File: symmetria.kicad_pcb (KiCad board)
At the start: 2 copper layers, 97 parts, among them J2 USB_C_Receptacle_USB2.0, SW1 SW_Push, U1 SRV05-4, U2 ATmega32U4-AU, Y1 16MHz

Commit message: PCB Laid out
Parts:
- added MX39: MX-NoLED, MX_Only:MXOnly-1.5U-NoLED, F.Cu at (774.7, 146.1)
- D1, D10, D11, D12, D13, D14, D15, D16, D17, D18, D19, D2, D20, D21, D22, D23, D24, D25, D26, D27, D28, D29, D3, D30, D31, D32, D33, D34, D35, D36, D37, D38, D39, D4, D5, D6, D7, D8, D9: moved to B.Cu
- moved D36 444.8 mm to (806.5, 127.0), turned to 90 degrees
- moved D24 439.4 mm to (806.5, 108.0), turned to 90 degrees
- moved D35 432.5 mm to (787.4, 127.0), turned to 90 degrees
- moved D12 431.7 mm to (806.5, 88.9), turned to 90 degrees
- moved D23 426.6 mm to (787.4, 108.0), turned to 90 degrees
- moved D39 424.8 mm to (782.6, 146.1), turned to 90 degrees
- moved D34 413.1 mm to (768.4, 127.0), turned to 90 degrees
- moved MX39 412.7 mm to (774.7, 146.1)
- moved MX36 411.8 mm to (798.5, 127.0)
- moved D11 408.1 mm to (787.4, 88.9), turned to 90 degrees
- moved D22 401.8 mm to (768.4, 108.0), turned to 90 degrees
- moved D10 396.5 mm to (768.4, 88.9), turned to 90 degrees
- moved MX24 392.2 mm to (798.5, 108.0)
- moved MX33 391.4 mm to (741.4, 127.0)
- moved MX34 386.9 mm to (760.4, 127.0)
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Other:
- board outline added: 254.4 x 90 mm

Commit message: PCB Laid out
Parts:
- moved R6 11.4 mm to (575.3, 84.5), turned to 180 degrees
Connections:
- net Net-(U2-Pad19) renamed ROW3
- U2 pad 20: Net-(U2-Pad20) -> ROW2
- U2 pad 21: Net-(U2-Pad21) -> ROW1
- U2 pad 22: Net-(U2-Pad22) -> ROW0
- U2 pad 25: Net-(U2-Pad25) -> COL0
- U2 pad 26: Net-(U2-Pad26) -> COL1
- U2 pad 27: Net-(U2-Pad27) -> COL2
- U2 pad 28: Net-(U2-Pad28) -> COL3
- U2 pad 29: Net-(U2-Pad29) -> COL4
- U2 pad 30: Net-(U2-Pad30) -> COL5
- U2 pad 31: Net-(U2-Pad31) -> COL6
- U2 pad 32: Net-(U2-Pad32) -> COL7
- U2 pad 36: Net-(U2-Pad36) -> COL8
- U2 pad 37: Net-(U2-Pad37) -> COL9
- U2 pad 38: Net-(U2-Pad38) -> COL10
- U2 pad 39: Net-(U2-Pad39) -> COL11
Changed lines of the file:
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@@
     (zones 0)
     (modules 98)
-    (nets 100)
+    (nets 85)
   )
   (page A4)
@@
   (net 75 "Net-(U2-Pad41)")
   (net 76 "Net-(U2-Pad40)")
-  (net 77 "Net-(U2-Pad39)")
-  (net 78 "Net-(U2-Pad38)")
-  (net 79 "Net-(U2-Pad37)")
-  (net 80 "Net-(U2-Pad36)")
-  (net 81 "Net-(U2-Pad32)")
-  (net 82 "Net-(U2-Pad31)")
-  (net 83 "Net-(U2-Pad30)")
-  (net 84 "Net-(U2-Pad29)")
-  (net 85 "Net-(U2-Pad28)")
-  (net 86 "Net-(U2-Pad27)")
-  (net 87 "Net-(U2-Pad26)")
-  (net 88 "Net-(U2-Pad25)")
-  (net 89 "Net-(U2-Pad22)")
-  (net 90 "Net-(U2-Pad21)")
-  (net 91 "Net-(U2-Pad20)")
-  (net 92 "Net-(U2-Pad19)")
-  (net 93 "Net-(U2-Pad18)")
-  (net 94 "Net-(U2-Pad12)")
-  (net 95 "Net-(U2-Pad11)")
-  (net 96 "Net-(U2-Pad10)")
-  (net 97 "Net-(U2-Pad9)")
-  (net 98 "Net-(U2-Pad8)")
-  (net 99 "Net-(U2-Pad1)")
+  (net 77 "Net-(U2-Pad18)")
+  (net 78 "Net-(U2-Pad12)")
+  (net 79 "Net-(U2-Pad11)")
+  (net 80 "Net-(U2-Pad10)")
+  (net 81 "Net-(U2-Pad9)")
+  (net 82 "Net-(U2-Pad8)")
+  (net 83 "Net-(U2-Pad1)")
+  (net 84 ROW3)
   (net_class Default "This is the default net class."
     (clearance 0.2)
@@
     (add_net "Net-(U2-Pad12)")
     (add_net "Net-(U2-Pad18)")
-    (add_net "Net-(U2-Pad19)")
-    (add_net "Net-(U2-Pad20)")
-    (add_net "Net-(U2-Pad21)")
-    (add_net "Net-(U2-Pad22)")
-    (add_net "Net-(U2-Pad25)")
-    (add_net "Net-(U2-Pad26)")
-    (add_net "Net-(U2-Pad27)")
-    (add_net "Net-(U2-Pad28)")
-    (add_net "Net-(U2-Pad29)")
-    (add_net "Net-(U2-Pad30)")
-    (add_net "Net-(U2-Pad31)")
-    (add_net "Net-(U2-Pad32)")
-    (add_net "Net-(U2-Pad36)")
-    (add_net "Net-(U2-Pad37)")
-    (add_net "Net-(U2-Pad38)")
-    (add_net "Net-(U2-Pad39)")
     (add_net "Net-(U2-Pad40)")
     (add_net "Net-(U2-Pad41)")
@@
     (add_net ROW1)
     (add_net ROW2)
+    (add_net ROW3)
     (add_net ROW4)
     (add_net VBUS)
@@
       (net 76 "Net-(U2-Pad40)"))
     (pad 39 smd rect (at 0 -5.7 90) (size 1.5 0.55) (layers F.Cu F.Paste F.Mask)
-      (net 77 "Net-(U2-Pad39)"))
+      (net 67 COL11))
     (pad 38 smd rect (at 0.8 -5.7 90) (size 1.5 0.55) (layers F.Cu F.Paste F.Mask)
-      (net 78 "Net-(U2-Pad38)"))
+      (net 66 COL10))
     (pad 37 smd rect (at 1.6 -5.7 90) (size 1.5 0.55) (layers F.Cu F.Paste F.Mask)
-      (net 79 "Net-(U2-Pad37)"))
+      (net 65 COL9))
     (pad 36 smd rect (at 2.4 -5.7 90) (size 1.5 0.55) (layers F.Cu F.Paste F.Mask)
-      (net 80 "Net-(U2-Pad36)"))
+      (net 64 COL8))
     (pad 35 smd rect (at 3.2 -5.7 90) (size 1.5 0.55) (layers F.Cu F.Paste F.Mask)
       (net 1 GND))
@@
       (net 73 "Net-(R6-Pad2)"))
     (pad 32 smd rect (at 5.7 -3.2) (size 1.5 0.55) (layers F.Cu F.Paste F.Mask)
-      (net 81 "Net-(U2-Pad32)"))
+      (net 63 COL7))
     (pad 31 smd rect (at 5.7 -2.4) (size 1.5 0.55) (layers F.Cu F.Paste F.Mask)
-      (net 82 "Net-(U2-Pad31)"))
+      (net 62 COL6))
     (pad 30 smd rect (at 5.7 -1.6) (size 1.5 0.55) (layers F.Cu F.Paste F.Mask)
-      (net 83 "Net-(U2-Pad30)"))
+      (net 61 COL5))
     (pad 29 smd rect (at 5.7 -0.8) (size 1.5 0.55) (layers F.Cu F.Paste F.Mask)
-      (net 84 "Net-(U2-Pad29)"))
+      (net 60 COL4))
     (pad 28 smd rect (at 5.7 0) (size 1.5 0.55) (layers F.Cu F.Paste F.Mask)
-      (net 85 "Net-(U2-Pad28)"))
+      (net 59 COL3))
     (pad 27 smd rect (at 5.7 0.8) (size 1.5 0.55) (layers F.Cu F.Paste F.Mask)
-      (net 86 "Net-(U2-Pad27)"))
+      (net 58 COL2))
     (pad 26 smd rect (at 5.7 1.6) (size 1.5 0.55) (layers F.Cu F.Paste F.Mask)
-      (net 87 "Net-(U2-Pad26)"))
+      (net 57 COL1))
     (pad 25 smd rect (at 5.7 2.4) (size 1.5 0.55) (layers F.Cu F.Paste F.Mask)
-      (net 88 "Net-(U2-Pad25)"))
+      (net 56 COL0))
     (pad 24 smd rect (at 5.7 3.2) (size 1.5 0.55) (layers F.Cu F.Paste F.Mask)
       (net 5 +5V))
@@
       (net 1 GND))
     (pad 22 smd rect (at 4 5.7 90) (size 1.5 0.55) (layers F.Cu F.Paste F.Mask)
-      (net 89 "Net-(U2-Pad22)"))
+      (net 7 ROW0))
     (pad 21 smd rect (at 3.2 5.7 90) (size 1.5 0.55) (layers F.Cu F.Paste F.Mask)
-      (net 90 "Net-(U2-Pad21)"))
+      (net 20 ROW1))
     (pad 20 smd rect (at 2.4 5.7 90) (size 1.5 0.55) (layers F.Cu F.Paste F.Mask)
-      (net 91 "Net-(U2-Pad20)"))
+      (net 33 ROW2))
     (pad 19 smd rect (at 1.6 5.7 90) (size 1.5 0.55) (layers F.Cu F.Paste F.Mask)
-      (net 92 "Net-(U2-Pad19)"))
+      (net 84 ROW3))
     (pad 18 smd rect (at 0.8 5.7 90) (size 1.5 0.55) (layers F.Cu F.Paste F.Mask)
-      (net 93 "Net-(U2-Pad18)"))
+      (net 77 "Net-(U2-Pad18)"))
     (pad 17 smd rect (at 0 5.7 90) (size 1.5 0.55) (layers F.Cu F.Paste F.Mask)
       (net 2 "Net-(C1-Pad1)"))
@@
       (net 68 "Net-(R3-Pad2)"))
     (pad 12 smd rect (at -4 5.7 90) (size 1.5 0.55) (layers F.Cu F.Paste F.Mask)
-      (net 94 "Net-(U2-Pad12)"))
+      (net 78 "Net-(U2-Pad12)"))
     (pad 11 smd rect (at -5.7 4) (size 1.5 0.55) (layers F.Cu F.Paste F.Mask)
-      (net 95 "Net-(U2-Pad11)"))
+      (net 79 "Net-(U2-Pad11)"))
     (pad 10 smd rect (at -5.7 3.2) (size 1.5 0.55) (layers F.Cu F.Paste F.Mask)
-      (net 96 "Net-(U2-Pad10)"))
+      (net 80 "Net-(U2-Pad10)"))
     (pad 9 smd rect (at -5.7 2.4) (size 1.5 0.55) (layers F.Cu F.Paste F.Mask)
-      (net 97 "Net-(U2-Pad9)"))
+      (net 81 "Net-(U2-Pad9)"))
     (pad 8 smd rect (at -5.7 1.6) (size 1.5 0.55) (layers F.Cu F.Paste F.Mask)
-      (net 98 "Net-(U2-Pad8)"))
+      (net 82 "Net-(U2-Pad8)"))
     (pad 7 smd rect (at -5.7 0.8) (size 1.5 0.55) (layers F.Cu F.Paste F.Mask)
       (net 5 +5V))
@@
       (net 5 +5V))
     (pad 1 smd rect (at -5.7 -4) (size 1.5 0.55) (layers F.Cu F.Paste F.Mask)
-      (net 99 "Net-(U2-Pad1)"))
+      (net 83 "Net-(U2-Pad1)"))
     (model ${KISYS3DMOD}/Package_QFP.3dshapes/TQFP-44_10x10mm_P0.8mm.wrl
       (at (xyz 0 0 0))
@@
   )
   (module Resistor_SMD:R_0805_2012Metric (layer F.Cu)
-    (at 575.183 95.8365 90)
+    (at 575.31 84.455 180)
     (descr "Resistor SMD 0805 (2012 Metric), square (rectangular) end terminal, IPC_7351 nominal, (Body size source: https://docs.google.com/spreadsheets/d/1BsfQQcO9C6DZCsRaXUlFlo91Tg2WpOkGARC1WS5S8t0/edit?usp=sharing), generated with kicad-footprint-generator")
     (tags resistor)
     (attr smd)
-    (fp_text reference R6 (at 0 -1.65 270) (layer F.SilkS)
-      (effects (font (size 1 1) (thickness 0.15)))
-    )
-    (fp_text value 10K (at 0 1.65 270) (layer F.Fab)
+    (fp_text reference R6 (at 0 -1.65 180) (layer F.SilkS)
+      (effects (font (size 1 1) (thickness 0.15)))
+    )
+    (fp_text value 10K (at 0 1.65 180) (layer F.Fab)
       (effects (font (size 1 1) (thickness 0.15)))
     )
@@
     (fp_line (start -1 -0.6) (end 1 -0.6) (layer F.Fab) (width 0.1))
     (fp_line (start -1 0.6) (end -1 -0.6) (layer F.Fab) (width 0.1))
-    (fp_text user %R (at 0 0 270) (layer F.Fab)
+    (fp_text user %R (at 0 0 180) (layer F.Fab)
       (effects (font (size 0.5 0.5) (thickness 0.08)))
     )
-    (pad 2 smd roundrect (at 0.9375 0 90) (size 0.975 1.4) (layers F.Cu F.Paste F.Mask) (roundrect_rratio 0.25)
+    (pad 2 smd roundrect (at 0.9375 0 180) (size 0.975 1.4) (layers F.Cu F.Paste F.Mask) (roundrect_rratio 0.25)
       (net 73 "Net-(R6-Pad2)"))
-    (pad 1 smd roundrect (at -0.9375 0 90) (size 0.975 1.4) (layers F.Cu F.Paste F.Mask) (roundrect_rratio 0.25)
+    (pad 1 smd roundrect (at -0.9375 0 180) (size 0.975 1.4) (layers F.Cu F.Paste F.Mask) (roundrect_rratio 0.25)
       (net 1 GND))
     (model ${KISYS3DMOD}/Resistor_SMD.3dshapes/R_0805_2012Metric.wrl

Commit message: Switch Tracing Complete
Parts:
- J2: moved to B.Cu
- moved C4 4.45 mm to (565.0, 112.3)
- turned J2 to 0 degrees
- turned U1 to 270 degrees
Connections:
- D37 pad 1: ROW4 -> ROW3
- D38 pad 1: ROW4 -> ROW3
- D39 pad 1: ROW4 -> ROW3
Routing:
- net COL10: track 0.00 -> 291.3 mm
- net COL11: track 0.00 -> 288.1 mm
- net ROW2: track 0.00 -> 283.2 mm, vias 0 -> 1
- net ROW1: track 0.00 -> 268.7 mm, vias 0 -> 1
- net ROW0: track 0.00 -> 266.7 mm, vias 0 -> 1
- net ROW3: track 0.00 -> 264.2 mm, vias 0 -> 1
- net COL9: track 0.00 -> 247.4 mm
- net COL8: track 0.00 -> 225.6 mm
- net COL6: track 0.00 -> 212.5 mm
- net COL7: track 0.00 -> 202.9 mm
- net COL5: track 0.00 -> 164.9 mm
- net COL4: track 0.00 -> 145.9 mm
- net COL3: track 0.00 -> 127.0 mm
- net COL1: track 0.00 -> 112.7 mm
- net COL2: track 0.00 -> 107.9 mm
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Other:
- outline, holes or cut-outs redrawn
- net class Default: trace_width 0.25 -> 0.254
- net class Power added: clearance 0.2, trace_width 0.381, via_dia 0.8, via_drill 0.4

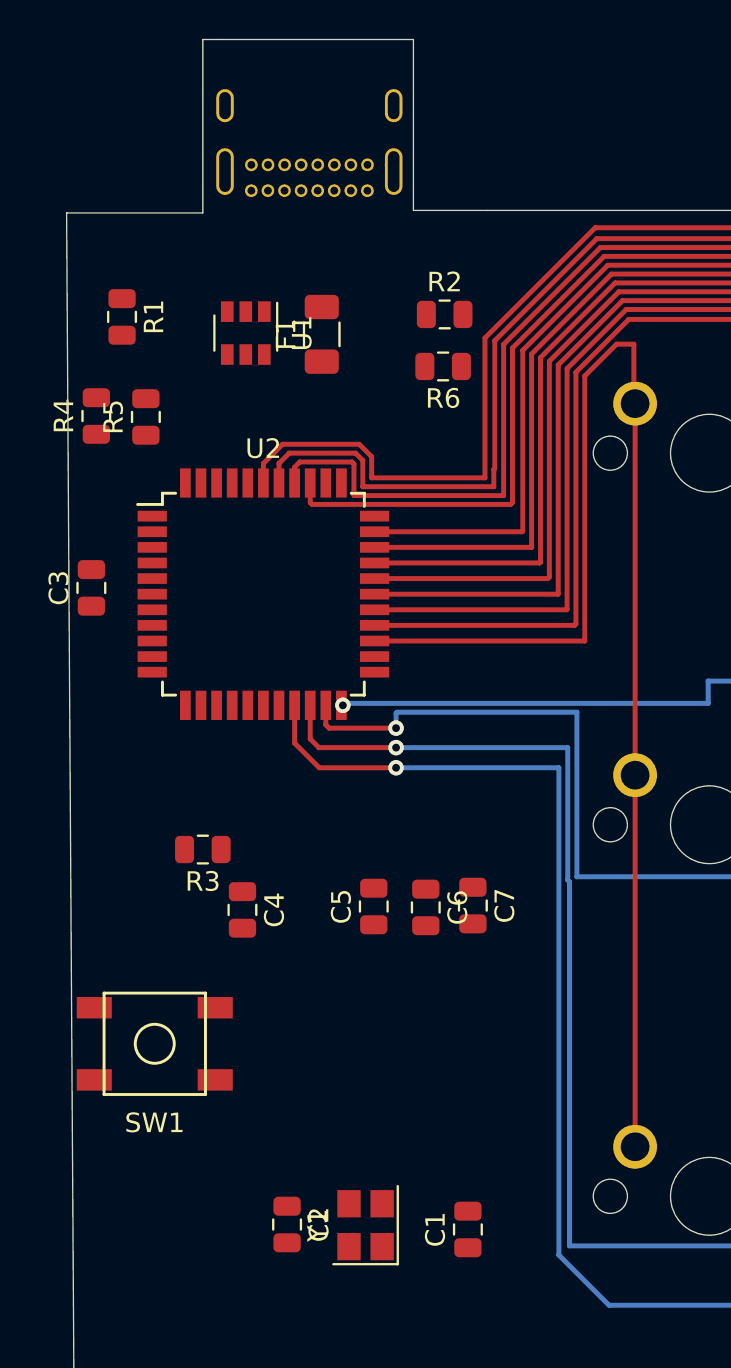
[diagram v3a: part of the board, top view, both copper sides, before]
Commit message: PCB routing Finished
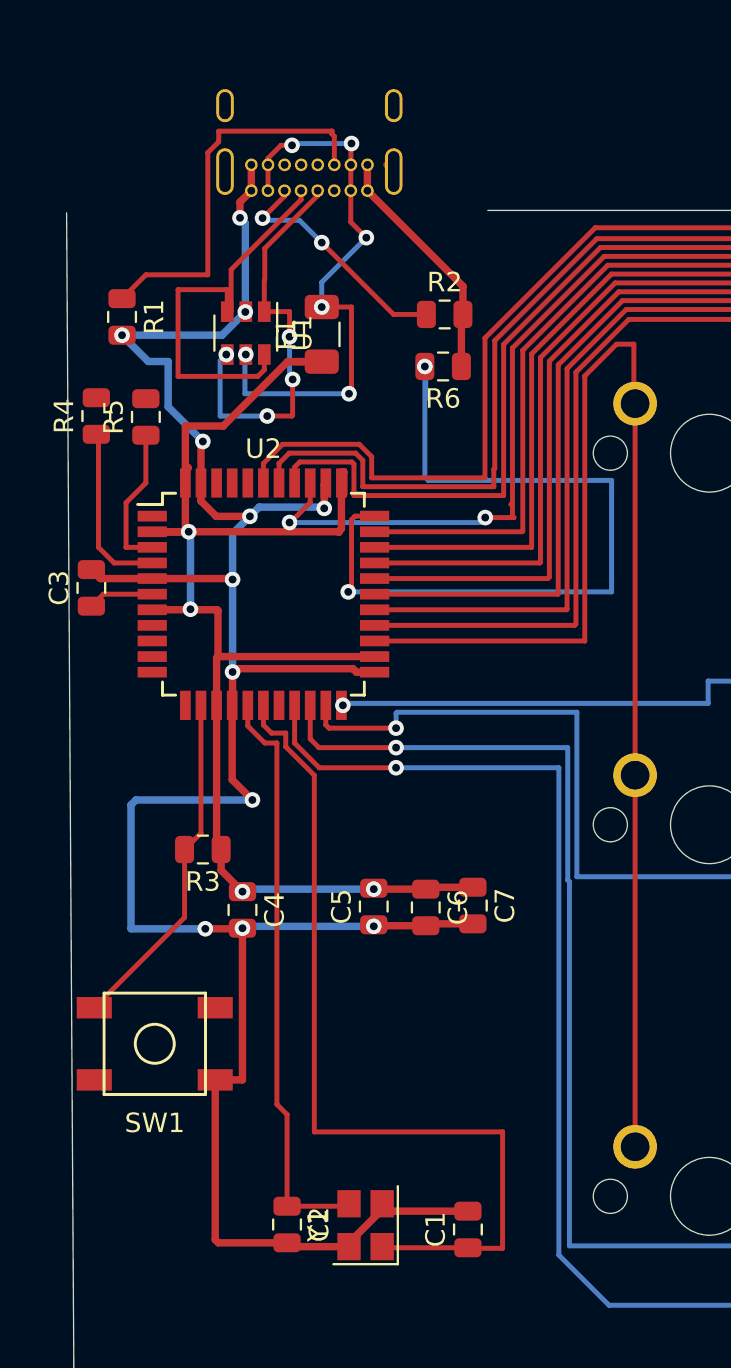
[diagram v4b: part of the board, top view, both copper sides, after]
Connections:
- R4 pad 2: D+ -> DBUS+
- R5 pad 2: D- -> DBUS-
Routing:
- net GND: track 0.71 -> 139.5 mm, vias 0 -> 12
- net +5V: track 0.00 -> 74.1 mm, vias 0 -> 4
- net Net-(C1-Pad1): track 0.00 -> 45.2 mm
- net Net-(R6-Pad2): track 0.00 -> 41.2 mm, vias 0 -> 2
- net Net-(C2-Pad1): track 0.00 -> 30.1 mm
- net VBUS: track 0.14 -> 29.9 mm, vias 0 -> 6
- net DBUS+: track 0.00 -> 21.3 mm
- net DBUS-: track 0.00 -> 21.1 mm, vias 0 -> 4
- net Net-(J2-PadB5): track 0.00 -> 20.1 mm
- net Net-(R3-Pad2): track 0.00 -> 17.8 mm
- net Net-(J2-PadA5): track 0.00 -> 12.3 mm, vias 0 -> 2
- net Net-(R4-Pad1): track 0.00 -> 8.93 mm
- net Net-(R5-Pad1): track 0.00 -> 7.51 mm
- net COL8: track 225.6 -> 229.1 mm, vias 0 -> 2
- net Net-(C3-Pad1): track 0.00 -> 3.37 mm
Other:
- board size 254.4 x 90 mm -> 254.4 x 81.3 mm
